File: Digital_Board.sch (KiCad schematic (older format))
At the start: 0 parts

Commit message: Connections were made to FPGA banks
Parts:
- added C?: C_Small, Capacitor_SMD:C_0603_1608Metric_Pad1.08x0.95mm_HandSolder, symbol Device:C_Small
- added C?: C_Polarized_Small, Capacitor_Tantalum_SMD:CP_EIA-1608-10_AVX-L_Pad1.25x1.05mm_HandSolder, symbol Device:C_Polarized_Small
- added C?: C_Small, symbol Device:C_Small
- added R? (x2): R_Small_US, Resistor_SMD:R_0603_1608Metric_Pad0.98x0.95mm_HandSolder, symbol Device:R_Small_US
- added TP?: TestPoint, TestPoint:TestPoint_Pad_2.0x2.0mm, symbol Connector:TestPoint
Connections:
- net labels added: GNDD, I2C2_SCL, I2C2_SDA, I2C_SCL, VCC3V3
- wire segments 112 -> 137

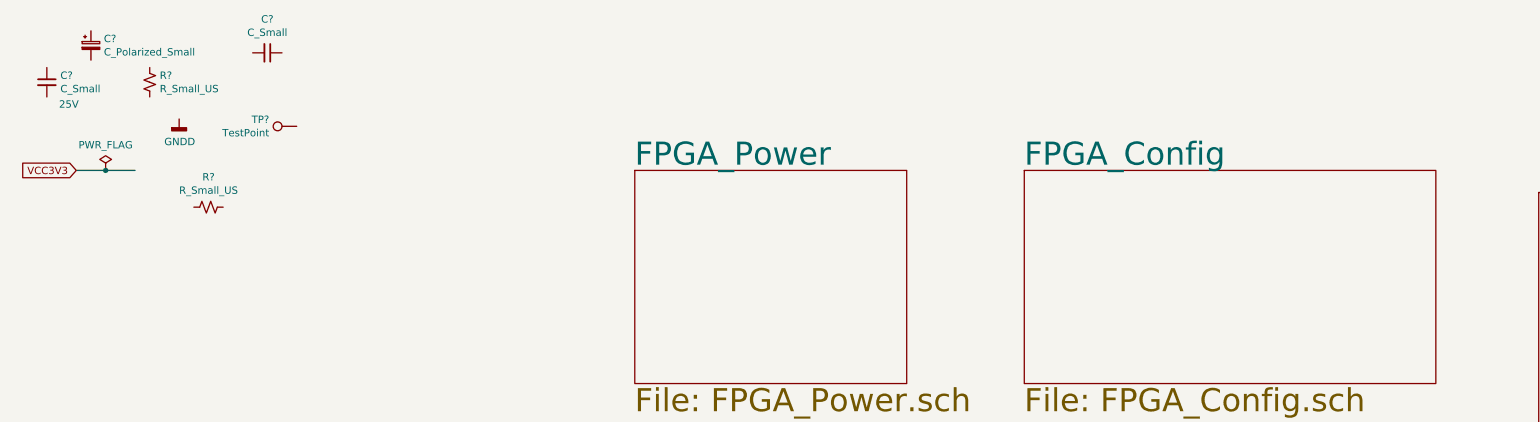
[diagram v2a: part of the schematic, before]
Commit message: Corrected PCB import errors
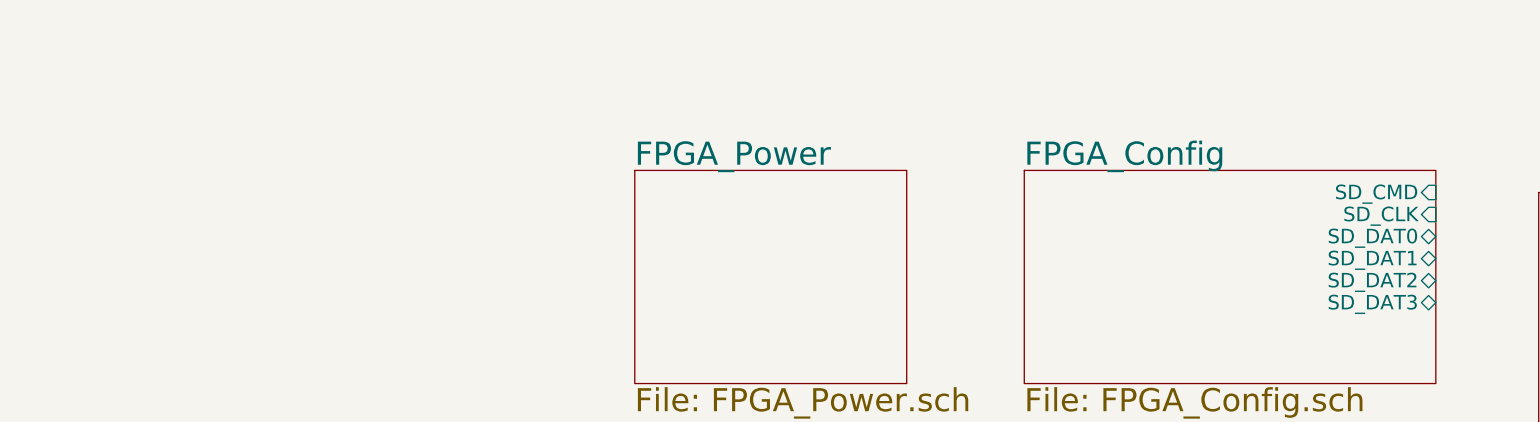
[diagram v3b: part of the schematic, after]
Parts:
- removed C?: C_Small, Capacitor_SMD:C_0603_1608Metric_Pad1.08x0.95mm_HandSolder, symbol Device:C_Small
- removed C?: C_Polarized_Small, Capacitor_Tantalum_SMD:CP_EIA-1608-10_AVX-L_Pad1.25x1.05mm_HandSolder, symbol Device:C_Polarized_Small
- removed C?: C_Small, symbol Device:C_Small
- removed R? (x2): R_Small_US, Resistor_SMD:R_0603_1608Metric_Pad0.98x0.95mm_HandSolder, symbol Device:R_Small_US
- removed TP?: TestPoint, TestPoint:TestPoint_Pad_2.0x2.0mm, symbol Connector:TestPoint
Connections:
- net labels removed: GNDD, VCC3V3
- wire segments 137 -> 135
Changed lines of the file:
@@
 F0 "FPGA_Config" 157
 F1 "FPGA_Config.sch" 157
+F2 "SD_CMD" I R 7500 1600 98
+F3 "SD_CLK" I R 7500 1750 98
+F4 "SD_DAT0" B R 7500 1900 98
+F5 "SD_DAT1" B R 7500 2050 98
+F6 "SD_DAT2" B R 7500 2200 98
+F7 "SD_DAT3" B R 7500 2350 98
 $EndSheet
 $Sheet
@@
 F2 "RTC_SCL" I L 15200 11500 50
 F3 "RTC_SDA" B L 15200 11600 50
-F5 "RTC_OSC_OUT" O L 15200 11700 50
-F6 "RTC_SQW" O L 15200 11800 50
-F7 "FAN_CTRL_PWM" I L 15200 12000 50
-F8 "12VIN" I R 16750 11500 50
+F4 "RTC_OSC_OUT" O L 15200 11700 50
+F5 "RTC_SQW" O L 15200 11800 50
+F6 "FAN_CTRL_PWM" I L 15200 12000 50
+F7 "12VIN" I R 16750 11500 50
 $EndSheet
 $Sheet
@@
 Wire Wire Line
 	15200 10600 14200 10600
-$Comp
-L Device:R_Small_US R?
-U 1 1 6076B72D
-P -1250 850
-AR Path="/601E7C5A/6076B72D" Ref="R?"  Part="1"
-AR Path="/601E7CC8/6076B72D" Ref="R?"  Part="1"
-AR Path="/601E7C92/6076B72D" Ref="R?"  Part="1"
-AR Path="/601E7C92/60257FE5/6076B72D" Ref="R?"  Part="1"
-AR Path="/601E7B38/6076B72D" Ref="R?"  Part="1"
-AR Path="/60256C5F/6076B72D" Ref="R?"  Part="1"
-AR Path="/6076B72D" Ref="R?"  Part="1"
-F 0 "R?" H -1182 896 50  0000 L CNN
-F 1 "R_Small_US" H -1182 805 50  0000 L CNN
-F 2 "Resistor_SMD:R_0603_1608Metric_Pad0.98x0.95mm_HandSolder" H -1250 850 50  0001 C CNN
-F 3 "~" H -1250 850 50  0001 C CNN
-	1    -1250 850
-	1    0    0    -1
-$EndComp
-$Comp
-L Device:C_Small C?
-U 1 1 6076B734
-P -1950 850
-AR Path="/601E7C5A/6076B734" Ref="C?"  Part="1"
-AR Path="/601E7CC8/6076B734" Ref="C?"  Part="1"
-AR Path="/601E7C92/6076B734" Ref="C?"  Part="1"
-AR Path="/601E7C92/60257FE5/6076B734" Ref="C?"  Part="1"
-AR Path="/601E7B38/6076B734" Ref="C?"  Part="1"
-AR Path="/60256C5F/6076B734" Ref="C?"  Part="1"
-AR Path="/6076B734" Ref="C?"  Part="1"
-F 0 "C?" H -1858 896 50  0000 L CNN
-F 1 "C_Small" H -1858 805 50  0000 L CNN
-F 2 "Capacitor_SMD:C_0603_1608Metric_Pad1.08x0.95mm_HandSolder" H -1950 850 50  0001 C CNN
-F 3 "~" H -1950 850 50  0001 C CNN
-F 4 "25V" H -1800 700 50  0000 C CNN "Voltage"
-	1    -1950 850
-	1    0    0    -1
-$EndComp
-Text GLabel -1750 1450 0    50   Input ~ 0
-VCC3V3
-$Comp
-L power:PWR_FLAG #FLG?
-U 1 1 6076B73B
-P -1550 1450
-AR Path="/601E7C5A/6076B73B" Ref="#FLG?"  Part="1"
-AR Path="/601E7CC8/6076B73B" Ref="#FLG?"  Part="1"
-AR Path="/601E7C92/6076B73B" Ref="#FLG?"  Part="1"
-AR Path="/601E7C92/60257FE5/6076B73B" Ref="#FLG?"  Part="1"
-AR Path="/601E7B38/6076B73B" Ref="#FLG?"  Part="1"
-AR Path="/60256C5F/6076B73B" Ref="#FLG?"  Part="1"
-AR Path="/6076B73B" Ref="#FLG?"  Part="1"
-F 0 "#FLG?" H -1550 1525 50  0001 C CNN
-F 1 "PWR_FLAG" H -1550 1623 50  0000 C CNN
-F 2 "" H -1550 1450 50  0001 C CNN
-F 3 "~" H -1550 1450 50  0001 C CNN
-	1    -1550 1450
-	1    0    0    -1
-$EndComp
-Connection ~ -1550 1450
-Wire Wire Line
-	-1550 1450 -1350 1450
-Wire Wire Line
-	-1750 1450 -1550 1450
-$Comp
-L power:GNDD #PWR?
-U 1 1 6076B744
-P -1050 1100
-AR Path="/601DF0A6/6076B744" Ref="#PWR?"  Part="1"
-AR Path="/601E7C5A/6076B744" Ref="#PWR?"  Part="1"
-AR Path="/601E7CC8/6076B744" Ref="#PWR?"  Part="1"
-AR Path="/601E7C92/6076B744" Ref="#PWR?"  Part="1"
-AR Path="/601E7C92/60257FE5/6076B744" Ref="#PWR?"  Part="1"
-AR Path="/601E7B38/6076B744" Ref="#PWR?"  Part="1"
-AR Path="/60256C5F/6076B744" Ref="#PWR?"  Part="1"
-AR Path="/6076B744" Ref="#PWR?"  Part="1"
-F 0 "#PWR?" H -1050 850 50  0001 C CNN
-F 1 "GNDD" H -1046 945 50  0000 C CNN
-F 2 "" H -1050 1100 50  0001 C CNN
-F 3 "" H -1050 1100 50  0001 C CNN
-	1    -1050 1100
-	1    0    0    -1
-$EndComp
-$Comp
-L Device:C_Polarized_Small C?
-U 1 1 6076B74B
-P -1650 600
-AR Path="/601E7C92/6076B74B" Ref="C?"  Part="1"
-AR Path="/601E7C92/60257FE5/6076B74B" Ref="C?"  Part="1"
-AR Path="/601E7B38/6076B74B" Ref="C?"  Part="1"
-AR Path="/60256C5F/6076B74B" Ref="C?"  Part="1"
-AR Path="/6076B74B" Ref="C?"  Part="1"
-F 0 "C?" H -1562 646 50  0000 L CNN
-F 1 "C_Polarized_Small" H -1562 555 50  0000 L CNN
-F 2 "Capacitor_Tantalum_SMD:CP_EIA-1608-10_AVX-L_Pad1.25x1.05mm_HandSolder" H -1650 600 50  0001 C CNN
-F 3 "~" H -1650 600 50  0001 C CNN
-F 4 "" H -1650 600 50  0000 C CNN "Voltage"
-	1    -1650 600
-	1    0    0    -1
-$EndComp
-$Comp
-L Device:C_Small C?
-U 1 1 6076B751
-P -450 650
-AR Path="/601E7B38/6076B751" Ref="C?"  Part="1"
-AR Path="/60256C5F/6076B751" Ref="C?"  Part="1"
-AR Path="/6076B751" Ref="C?"  Part="1"
-F 0 "C?" V -679 650 50  0000 C CNN
-F 1 "C_Small" V -588 650 50  0000 C CNN
-F 2 "" H -450 650 50  0001 C CNN
-F 3 "~" H -450 650 50  0001 C CNN
-	1    -450 650
-	0    1    1    0
-$EndComp
-$Comp
-L Device:R_Small_US R?
-U 1 1 6076B757
-P -850 1700
-AR Path="/60256C5F/6076B757" Ref="R?"  Part="1"
-AR Path="/6076B757" Ref="R?"  Part="1"
-F 0 "R?" V -1055 1700 50  0000 C CNN
-F 1 "R_Small_US" V -964 1700 50  0000 C CNN
-F 2 "Resistor_SMD:R_0603_1608Metric_Pad0.98x0.95mm_HandSolder" H -850 1700 50  0001 C CNN
-F 3 "~" H -850 1700 50  0001 C CNN
-	1    -850 1700
-	0    1    1    0
-$EndComp
-$Comp
-L Connector:TestPoint TP?
-U 1 1 6078C1B8
-P -250 1150
-AR Path="/6078C1B8" Ref="TP?"  Part="1"
-AR Path="/601E7CC8/6078C1B8" Ref="TP?"  Part="1"
-F 0 "TP?" V -204 1337 50  0000 L CNN
-F 1 "TestPoint" V -295 1337 50  0000 L CNN
-F 2 "TestPoint:TestPoint_Pad_2.0x2.0mm" H -50 1150 50  0001 C CNN
-F 3 "~" H -50 1150 50  0001 C CNN
-	1    -250 1150
-	0    -1   -1   0
-$EndComp
 Wire Wire Line
 	15200 11500 14200 11500
